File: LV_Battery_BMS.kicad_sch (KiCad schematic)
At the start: 53 parts, among them Q3 Q_NMOS_DGS

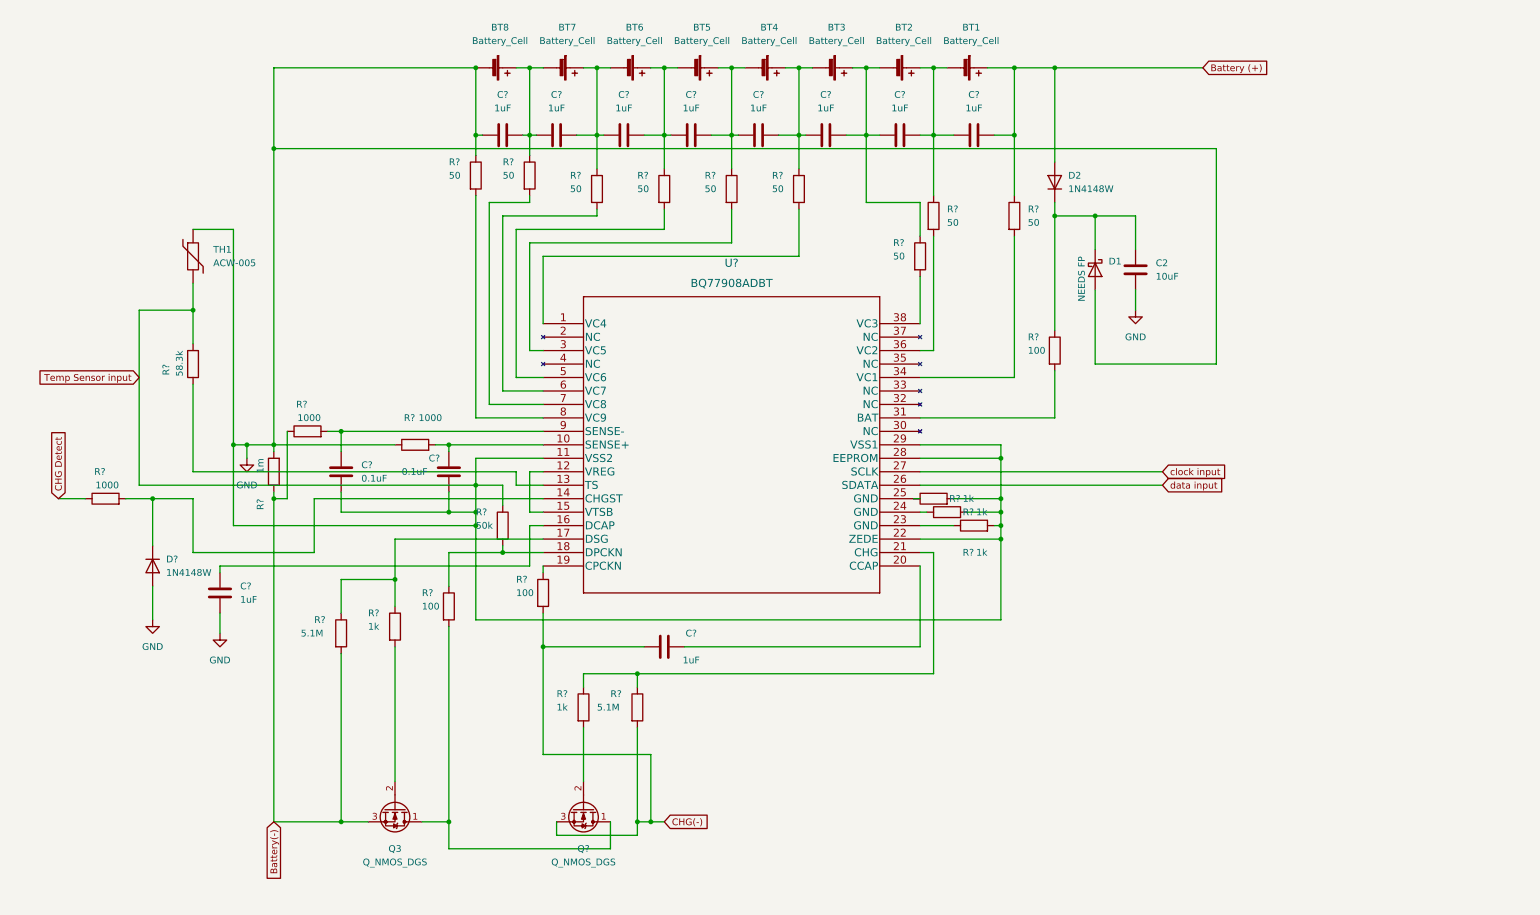
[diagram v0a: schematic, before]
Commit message: added uC, switch to BQ76930
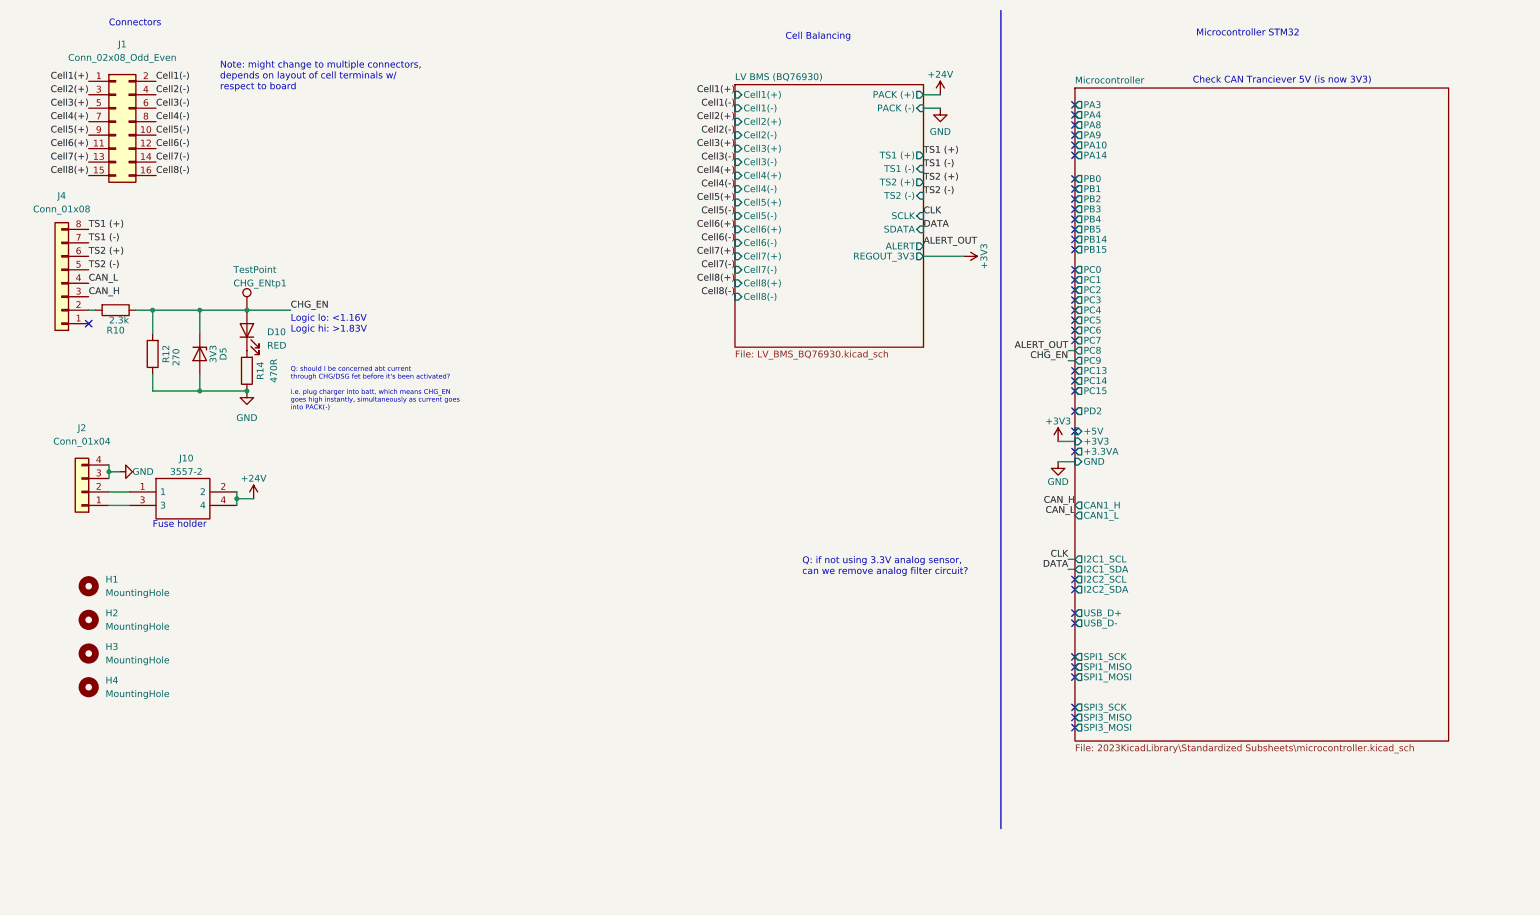
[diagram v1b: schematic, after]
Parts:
- removed BT1, BT2, BT3, BT4, BT5, BT6, BT7, BT8: Battery_Cell, symbol Device:Battery_Cell
- removed C2: 10uF, symbol Device:C
- removed C? (x10): 1uF, symbol Device:C
- removed C? (x2): 0.1uF, symbol Device:C
- removed D1: NEEDS FP, Diode_THT:D_DO-35_SOD27_P7.62mm_Horizontal, symbol Diode:1N5711
- removed D2, D?: 1N4148W, Diode_SMD:D_SOD-123, symbol Diode:1N4148W
- removed Q3, Q?: Q_NMOS_DGS, symbol Device:Q_NMOS_DGS
- removed R?: 50k, symbol Device:R
- removed R? (x5): 1k, symbol Device:R
- removed R? (x3): 100, symbol Device:R
- removed R? (x9): 50, symbol Device:R
- removed R? (x3): 1000, symbol Device:R
- removed R? (x2): 5.1M, symbol Device:R
- removed R?: 58.3k, symbol Device:R
- removed R?: 1m, symbol Device:R
- removed TH1: ACW-005, symbol Device:Thermistor
- removed U?: BQ77908ADBT, Global Libraries:SOP50P640X120-38N, symbol Custom Symbols:BQ77908ADBT
- added CHG_ENtp1: TestPoint, TestPoint:TestPoint_THTPad_D1.5mm_Drill0.7mm, symbol Connector:TestPoint
- added D10: RED, LED_SMD:LED_0603_1608Metric_Pad1.05x0.95mm_HandSolder, symbol Device:LED
- added D5: 3V3, Diode_SMD:D_SOD-323, symbol Device:D_Zener
- added H1, H2, H3, H4: MountingHole, MountingHole:MountingHole_3.2mm_M3_Pad, symbol Mechanical:MountingHole
- added J1: Conn_02x08_Odd_Even, Connector_Molex:Molex_Micro-Fit_3.0_43045-1600_2x08_P3.00mm_Horizontal, symbol Connector_Generic:Conn_02x08_Odd_Even
- added J10: 3557-2, SamacSys_Parts:3557-2, symbol SamacSys_Parts:3557-2
- added J2: Conn_01x04, Connector_Molex:Molex_Micro-Fit_3.0_43650-0400_1x04_P3.00mm_Horizontal, symbol Connector_Generic:Conn_01x04
- added J4: Conn_01x08, Connector_Molex:Molex_Micro-Fit_3.0_43045-0800_2x04_P3.00mm_Horizontal, symbol Connector_Generic:Conn_01x08
- added R10: 2.3k, Resistor_SMD:R_0603_1608Metric, symbol Device:R
- added R12: 270, Resistor_SMD:R_0603_1608Metric, symbol Device:R
- added R14: 470R, Resistor_SMD:R_0603_1608Metric_Pad0.98x0.95mm_HandSolder, symbol Device:R
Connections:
- net GND: now also D5.2 (A), J2.3 (Pin_3), J2.4 (Pin_4), R12.1, R14.1
- new net: J4.2 (Pin_2), R10.2
- new net: J10.1, J2.2 (Pin_2)
- new net: J10.3, J2.1 (Pin_1)
- new net: D10.1 (K), R14.2
- new net +24V: J10.2, J10.4
- new net CAN_H: J4.3 (Pin_3)
- new net CAN_L: J4.4 (Pin_4)
- new net CHG_EN: CHG_ENtp1.1, D10.2 (A), D5.1 (K), R10.1, R12.2
- new net Cell1(+): J1.1 (Pin_1)
- new net Cell1(-): J1.2 (Pin_2)
- new net Cell2(+): J1.3 (Pin_3)
- new net Cell2(-): J1.4 (Pin_4)
- new net Cell3(+): J1.5 (Pin_5)
- new net Cell3(-): J1.6 (Pin_6)
- new net Cell4(+): J1.7 (Pin_7)
- new net Cell4(-): J1.8 (Pin_8)
- new net Cell5(+): J1.9 (Pin_9)
- new net Cell5(-): J1.10 (Pin_10)
- new net Cell6(+): J1.11 (Pin_11)
- new net Cell6(-): J1.12 (Pin_12)
- new net Cell7(+): J1.13 (Pin_13)
- new net Cell7(-): J1.14 (Pin_14)
- new net Cell8(+): J1.15 (Pin_15)
- new net Cell8(-): J1.16 (Pin_16)
- new net TS1 (+): J4.8 (Pin_8)
- new net TS1 (-): J4.7 (Pin_7)
- new net TS2 (+): J4.6 (Pin_6)
- new net TS2 (-): J4.5 (Pin_5)
- no-connect marks 0 -> 39
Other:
- added sheet LV BMS (BQ76930) (LV_BMS_BQ76930.kicad_sch)
- added sheet Microcontroller (2023KicadLibrary\Standardized Subsheets\microcontroller.kicad_sch)
- note added: "Cell Balancing"
- note added: "Check CAN Tranciever 5V (is now 3V3)"
- note added: "Connectors"
- note added: "Fuse holder"
- note added: "Logic lo: <1.16V Logic hi: >1.83V"
- note added: "Microcontroller STM32"
- note added: "Note: might change to multiple connectors, depends on layout of cell terminals w/ respect to board"
- note added: "Q: if not using 3.3V analog sensor, can we remove analog filter circuit?"
- note added: "Q: should I be concerned abt current through CHG/DSG fet before it's been activated? i.e. plug charger into batt, which means CHG_EN goes high instantly, simultaneously as current goes into PACK(-)"
